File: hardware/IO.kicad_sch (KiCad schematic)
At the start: 30 parts, among them J1 Conn_01x04, J2 Screw_Terminal_01x07, J3 Screw_Terminal_01x02, J4 Screw_Terminal_01x04, J5 Conn_02x03_Odd_Even, J6 Conn_01x07, Q5 RE1C002UNTCL, Q6 RE1C002UNTCL, Q7 RE1C002UNTCL, Q8 RE1C002UNTCL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

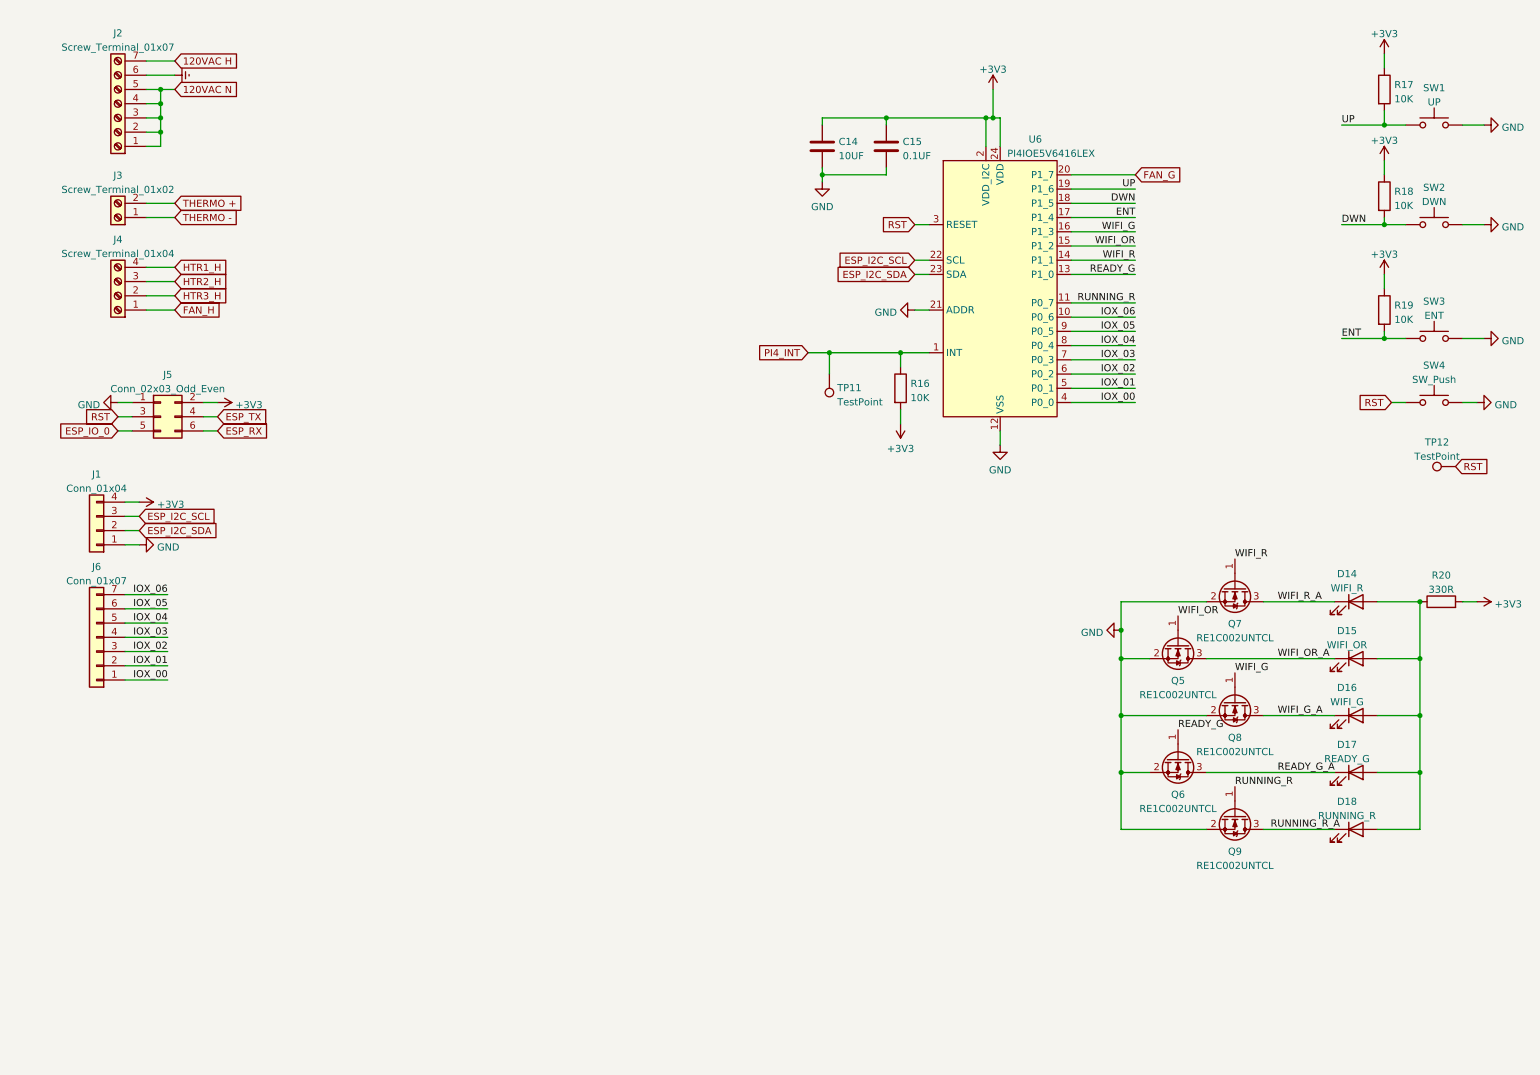
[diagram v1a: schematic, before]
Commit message: updated hardware schimatics for better readability
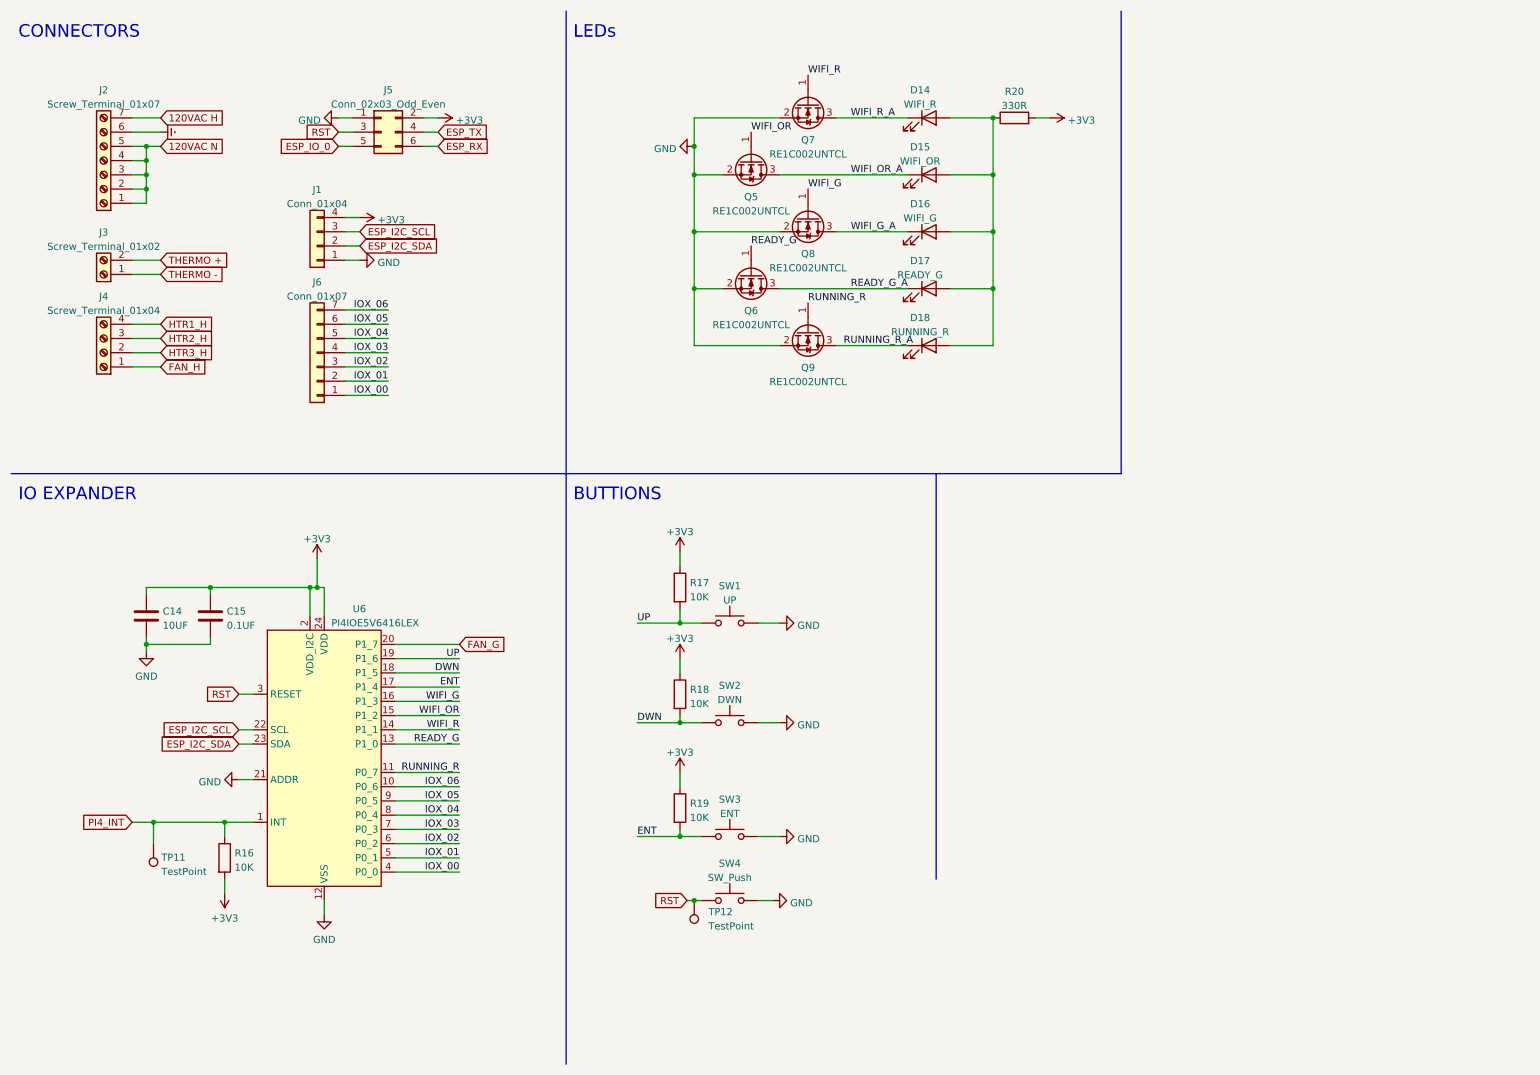
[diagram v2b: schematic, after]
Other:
- note added: "BUTTIONS"
- note added: "CONNECTORS"
- note added: "IO EXPANDER"
- note added: "LEDs"
- moved on the sheet: C14, C15, D14, D15, D16, D17, D18, J1, J2, J3, J4, J5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

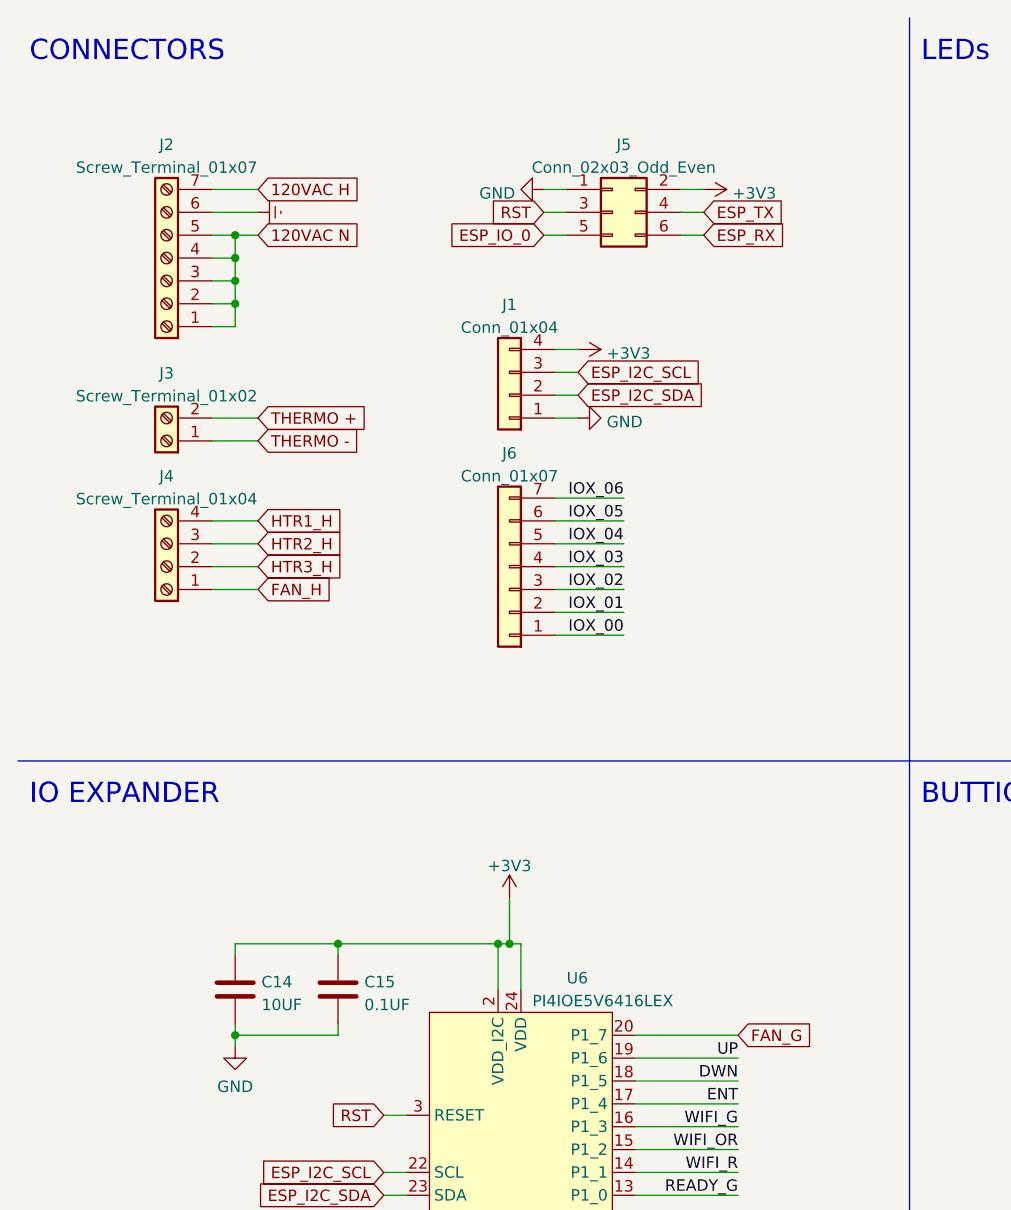
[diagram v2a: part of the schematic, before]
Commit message: added a voltage devider for the dcinput on the esp
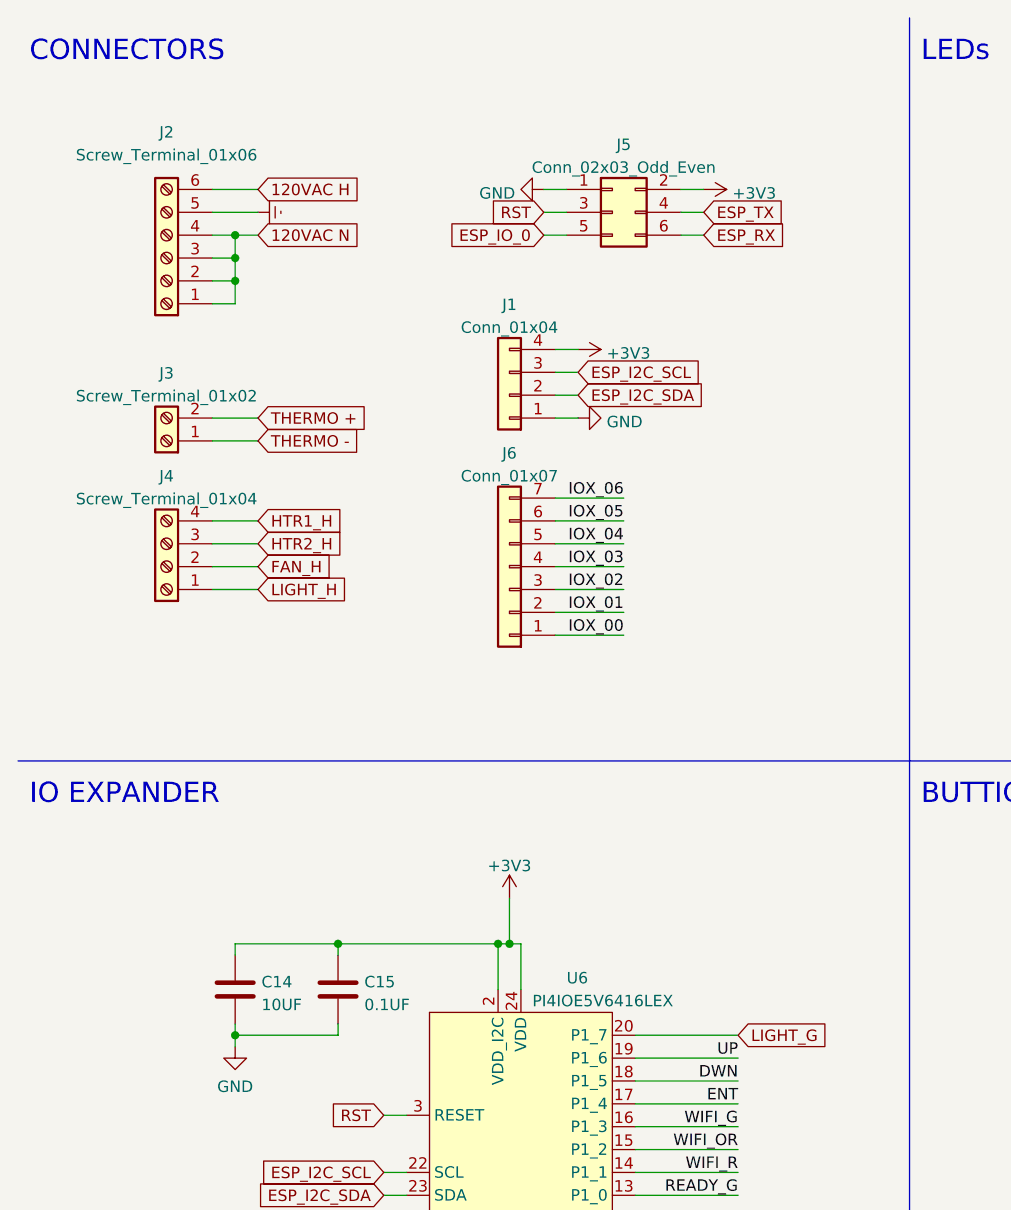
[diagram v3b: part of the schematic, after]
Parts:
- removed J2: Screw_Terminal_01x07, EXTRA:SCREW_TERM_5MM_7, symbol Connector:Screw_Terminal_01x07
- added J2: Screw_Terminal_01x06, symbol Connector:Screw_Terminal_01x06
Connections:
- net HTR3_H is gone; now on net FAN_H: J4.2 (Pin_2)
- net 120VAC H: now also J2.6 (Pin_6)
- net 120VAC N: now also J2.1 (Pin_1), J2.2 (Pin_2), J2.3 (Pin_3), J2.4 (Pin_4)
- net Earth: now also J2.5 (Pin_5)
- net FAN_H: no longer J4.1 (Pin_1)
- net FAN_G renamed LIGHT_G
- new net LIGHT_H: J4.1 (Pin_1)
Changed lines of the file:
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@@
   (junction (at 35.56 38.1) (diameter 0) (color 0 0 0 0)
   )
-  (junction (at 35.56 43.18) (diameter 0) (color 0 0 0 0)
-  )
   (junction (at 186.69 50.8) (diameter 0) (color 0 0 0 0)
   )
@@
     (stroke (width 0) (type default) (color 0 0 0 0))
   )
-  (wire (pts (xy 35.56 43.18) (xy 35.56 45.72))
-    (stroke (width 0) (type default) (color 0 0 0 0))
-  )
   (wire (pts (xy 158.75 71.12) (xy 171.45 71.12))
     (stroke (width 0) (type default) (color 0 0 0 0))
@@
   )
   (wire (pts (xy 134.62 170.18) (xy 133.35 170.18))
-    (stroke (width 0) (type default) (color 0 0 0 0))
-  )
-  (wire (pts (xy 35.56 45.72) (xy 33.02 45.72))
     (stroke (width 0) (type default) (color 0 0 0 0))
   )
@@
     )
   )
-  (global_label "FAN_H" (shape input) (at 38.1 74.93 0) (fields_autoplaced)
+  (global_label "LIGHT_H" (shape input) (at 38.1 74.93 0) (fields_autoplaced)
     (effects (font (size 1.27 1.27)) (justify left))
     (property "Intersheet References" "${INTERSHEET_REFS}" (id 0) (at 46.3188 74.8506 0)
@@
     )
   )
-  (global_label "FAN_G" (shape input) (at 91.44 124.46 0) (fields_autoplaced)
+  (global_label "LIGHT_G" (shape input) (at 91.44 124.46 0) (fields_autoplaced)
     (effects (font (size 1.27 1.27)) (justify left))
     (property "Intersheet References" "${INTERSHEET_REFS}" (id 0) (at 99.5983 124.3806 0)
@@
     )
   )
-  (global_label "HTR3_H" (shape input) (at 38.1 72.39 0) (fields_autoplaced)
+  (global_label "FAN_H" (shape input) (at 38.1 72.39 0) (fields_autoplaced)
     (effects (font (size 1.27 1.27)) (justify left))
     (property "Intersheet References" "${INTERSHEET_REFS}" (id 0) (at 47.5888 72.3106 0)
@@
     )
     (pin "1")
+  )
+  (symbol (lib_id "Connector:Screw_Terminal_01x06") (at 27.94 38.1 180) (unit 1)
+    (in_bom yes) (on_board yes) (fields_autoplaced)
+    (property "Reference" "J2" (id 0) (at 27.94 24.13 0))
+    (property "Value" "Screw_Terminal_01x06" (id 1) (at 27.94 26.67 0))
+    (property "Footprint" "" (id 2) (at 27.94 38.1 0)
+      (effects (font (size 1.27 1.27)) hide)
+    )
+    (property "Datasheet" "~" (id 3) (at 27.94 38.1 0)
+      (effects (font (size 1.27 1.27)) hide)
+    )
+    (pin "1")
+    (pin "2")
+    (pin "3")
+    (pin "4")
+    (pin "5")
+    (pin "6")
   )
   (symbol (lib_id "power:+3V3") (at 73.66 48.26 270) (unit 1)
@@
     (pin "2")
   )
-  (symbol (lib_id "Connector:Screw_Terminal_01x07") (at 27.94 38.1 180) (unit 1)
-    (in_bom yes) (on_board yes) (fields_autoplaced)
-    (property "Reference" "J2" (id 0) (at 27.94 25.5102 0))
-    (property "Value" "Screw_Terminal_01x07" (id 1) (at 27.94 28.0471 0))
-    (property "Footprint" "EXTRA:SCREW_TERM_5MM_7" (id 2) (at 27.94 38.1 0)
-      (effects (font (size 1.27 1.27)) hide)
-    )
-    (property "Datasheet" "~" (id 3) (at 27.94 38.1 0)
-      (effects (font (size 1.27 1.27)) hide)
-    )
-    (pin "1")
-    (pin "2")
-    (pin "3")
-    (pin "4")
-    (pin "5")
-    (pin "6")
-    (pin "7")
-  )
   (symbol (lib_id "Device:C") (at 46.99 119.38 0) (unit 1)

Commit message: more hardware revisions
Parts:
- J2: footprint (none) -> EXTRA:SCREW_TERM_5MM_7
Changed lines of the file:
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@@
     (property "Reference" "J2" (id 0) (at 27.94 24.13 0))
     (property "Value" "Screw_Terminal_01x06" (id 1) (at 27.94 26.67 0))
-    (property "Footprint" "" (id 2) (at 27.94 38.1 0)
+    (property "Footprint" "EXTRA:SCREW_TERM_5MM_7" (id 2) (at 27.94 38.1 0)
       (effects (font (size 1.27 1.27)) hide)
     )

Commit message: minor hardware refactoring & added firmware fuction
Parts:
- added R30, R31, R32, R33: 330R, Resistor_SMD:R_0603_1608Metric, symbol Device:R
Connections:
- net +3V3: now also R30.2, R31.2, R32.2, R33.2
- new net: D18.2 (A), R33.1
- new net: D15.2 (A), R30.1
- new net: D16.2 (A), R31.1
- new net: D17.2 (A), R32.1
- new net: D14.2 (A), R20.1
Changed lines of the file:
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@@
     (rev "B")
   )
-  (junction (at 186.69 60.96) (diameter 0) (color 0 0 0 0)
+  (junction (at 194.31 60.96) (diameter 0) (color 0 0 0 0)
   )
   (junction (at 130.81 158.75) (diameter 0) (color 0 0 0 0)
@@
   (junction (at 130.81 138.43) (diameter 0) (color 0 0 0 0)
   )
+  (junction (at 194.31 50.8) (diameter 0) (color 0 0 0 0)
+  )
   (junction (at 35.56 40.64) (diameter 0) (color 0 0 0 0)
   )
@@
   (junction (at 35.56 38.1) (diameter 0) (color 0 0 0 0)
   )
-  (junction (at 186.69 50.8) (diameter 0) (color 0 0 0 0)
-  )
-  (junction (at 186.69 30.48) (diameter 0) (color 0 0 0 0)
-  )
   (junction (at 133.35 35.56) (diameter 0) (color 0 0 0 0)
   )
@@
   (junction (at 35.56 35.56) (diameter 0) (color 0 0 0 0)
   )
-  (junction (at 186.69 40.64) (diameter 0) (color 0 0 0 0)
-  )
   (junction (at 133.35 60.96) (diameter 0) (color 0 0 0 0)
   )
@@
   (junction (at 133.35 170.18) (diameter 0) (color 0 0 0 0)
   )
+  (junction (at 194.31 40.64) (diameter 0) (color 0 0 0 0)
+  )
+  (junction (at 194.31 30.48) (diameter 0) (color 0 0 0 0)
+  )
   (wire (pts (xy 80.01 162.56) (xy 91.44 162.56))
     (stroke (width 0) (type default) (color 0 0 0 0))
@@
     (stroke (width 0) (type default) (color 0 0 0 0))
   )
+  (wire (pts (xy 194.31 30.48) (xy 194.31 40.64))
+    (stroke (width 0) (type default) (color 0 0 0 0))
+  )
   (wire (pts (xy 52.07 142.24) (xy 54.61 142.24))
     (stroke (width 0) (type default) (color 0 0 0 0))
@@
     (stroke (width 0) (type default) (color 0 0 0 0))
   )
-  (wire (pts (xy 186.69 30.48) (xy 186.69 40.64))
-    (stroke (width 0) (type default) (color 0 0 0 0))
-  )
   (wire (pts (xy 123.19 138.43) (xy 130.81 138.43))
     (stroke (width 0) (type default) (color 0 0 0 0))
@@
     (stroke (width 0) (type default) (color 0 0 0 0))
   )
+  (wire (pts (xy 194.31 40.64) (xy 194.31 50.8))
+    (stroke (width 0) (type default) (color 0 0 0 0))
+  )
+  (wire (pts (xy 194.31 50.8) (xy 194.31 60.96))
+    (stroke (width 0) (type default) (color 0 0 0 0))
+  )
   (wire (pts (xy 123.19 158.75) (xy 130.81 158.75))
     (stroke (width 0) (type default) (color 0 0 0 0))
@@
     (stroke (width 0) (type default) (color 0 0 0 0))
   )
+  (wire (pts (xy 194.31 60.96) (xy 194.31 71.12))
+    (stroke (width 0) (type default) (color 0 0 0 0))
+  )
   (wire (pts (xy 123.19 120.65) (xy 130.81 120.65))
     (stroke (width 0) (type default) (color 0 0 0 0))
@@
     (stroke (width 0) (type default) (color 0 0 0 0))
   )
-  (wire (pts (xy 186.69 40.64) (xy 186.69 50.8))
-    (stroke (width 0) (type default) (color 0 0 0 0))
-  )
   (wire (pts (xy 80.01 127) (xy 91.44 127))
     (stroke (width 0) (type default) (color 0 0 0 0))
@@
     (stroke (width 0) (type default) (color 0 0 0 0))
   )
-  (wire (pts (xy 186.69 60.96) (xy 186.69 71.12))
-    (stroke (width 0) (type default) (color 0 0 0 0))
-  )
   (wire (pts (xy 35.56 124.46) (xy 35.56 125.73))
     (stroke (width 0) (type default) (color 0 0 0 0))
@@
   )
   (wire (pts (xy 71.12 72.39) (xy 78.74 72.39))
-    (stroke (width 0) (type default) (color 0 0 0 0))
-  )
-  (wire (pts (xy 186.69 50.8) (xy 186.69 60.96))
     (stroke (width 0) (type default) (color 0 0 0 0))
   )
@@
     )
     (pin "1")
+  )
+  (symbol (lib_id "Device:R") (at 190.5 71.12 90) (unit 1)
+    (in_bom yes) (on_board yes) (fields_autoplaced)
+    (property "Reference" "R33" (id 0) (at 190.5 66.4042 90))
+    (property "Value" "330R" (id 1) (at 190.5 68.9411 90))
+    (property "Footprint" "Resistor_SMD:R_0603_1608Metric" (id 2) (at 190.5 72.898 90)
+      (effects (font (size 1.27 1.27)) hide)
+    )
+    (property "Datasheet" "~" (id 3) (at 190.5 71.12 0)
+      (effects (font (size 1.27 1.27)) hide)
+    )
+    (pin "1")
+    (pin "2")
   )
   (symbol (lib_name "BUK7M6R3-40EX_2") (lib_id "Transistor_FET:BUK7M6R3-40EX") (at 153.67 68.58 270) (unit 1)
@@
     (pin "3")
   )
+  (symbol (lib_id "Device:R") (at 190.5 50.8 90) (unit 1)
+    (in_bom yes) (on_board yes) (fields_autoplaced)
+    (property "Reference" "R31" (id 0) (at 190.5 46.0842 90))
+    (property "Value" "330R" (id 1) (at 190.5 48.6211 90))
+    (property "Footprint" "Resistor_SMD:R_0603_1608Metric" (id 2) (at 190.5 52.578 90)
+      (effects (font (size 1.27 1.27)) hide)
+    )
+    (property "Datasheet" "~" (id 3) (at 190.5 50.8 0)
+      (effects (font (size 1.27 1.27)) hide)
+    )
+    (pin "1")
+    (pin "2")
+  )
   (symbol (lib_name "BUK7M6R3-40EX_2") (lib_id "Transistor_FET:BUK7M6R3-40EX") (at 143.51 58.42 270) (unit 1)
     (in_bom yes) (on_board yes) (fields_autoplaced)
@@
     (pin "2")
   )
+  (symbol (lib_id "Device:R") (at 190.5 40.64 90) (unit 1)
+    (in_bom yes) (on_board yes) (fields_autoplaced)
+    (property "Reference" "R30" (id 0) (at 190.5 35.9242 90))
+    (property "Value" "330R" (id 1) (at 190.5 38.4611 90))
+    (property "Footprint" "Resistor_SMD:R_0603_1608Metric" (id 2) (at 190.5 42.418 90)
+      (effects (font (size 1.27 1.27)) hide)
+    )
+    (property "Datasheet" "~" (id 3) (at 190.5 40.64 0)
+      (effects (font (size 1.27 1.27)) hide)
+    )
+    (pin "1")
+    (pin "2")
+  )
   (symbol (lib_id "Device:LED") (at 175.26 60.96 0) (unit 1)
     (in_bom yes) (on_board yes) (fields_autoplaced)
@@
     (pin "1")
   )
+  (symbol (lib_id "Device:R") (at 190.5 60.96 90) (unit 1)
+    (in_bom yes) (on_board yes) (fields_autoplaced)
+    (property "Reference" "R32" (id 0) (at 190.5 56.2442 90))
+    (property "Value" "330R" (id 1) (at 190.5 58.7811 90))
+    (property "Footprint" "Resistor_SMD:R_0603_1608Metric" (id 2) (at 190.5 62.738 90)
+      (effects (font (size 1.27 1.27)) hide)
+    )
+    (property "Datasheet" "~" (id 3) (at 190.5 60.96 0)
+      (effects (font (size 1.27 1.27)) hide)
+    )
+    (pin "1")
+    (pin "2")
+  )
   (symbol (lib_id "Device:R") (at 190.5 30.48 90) (unit 1)
